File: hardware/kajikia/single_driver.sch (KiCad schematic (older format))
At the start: 17 parts

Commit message: reorder
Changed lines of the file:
@@
 $Descr A4 11693 8268
 encoding utf-8
-Sheet 2 11
+Sheet 6 8
 Title ""
 Date ""
@@
 U 1 1 5AF72EC0
 P 3500 2050
+AR Path="/5AF71FC6/5AF72EC0" Ref="JP1"  Part="1"
+AR Path="/5B406A82/5B411670/5AF72EC0" Ref="JP1"  Part="1"
 F 0 "JP1" H 3500 2255 50  0000 C CNN
 F 1 "SolderJumper_3_Open" H 3500 2164 50  0000 C CNN
@@
 U 1 1 5B028F12
 P 5950 3300
+AR Path="/5AF71FC6/5B028F12" Ref="U?"  Part="1"
+AR Path="/5B406A82/5B411670/5B028F12" Ref="U?"  Part="1"
 F 0 "U?" H 6950 1850 50  0000 C CNN
 F 1 "TMC5160-TA" H 6950 1750 50  0000 C CNN
@@
 U 1 1 5B03C5CD
 P 5950 4900
+AR Path="/5AF71FC6/5B03C5CD" Ref="#PWR0105"  Part="1"
+AR Path="/5B406A82/5B411670/5B03C5CD" Ref="#PWR0105"  Part="1"
 F 0 "#PWR0105" H 5950 4650 50  0001 C CNN
 F 1 "GND" H 5955 4727 50  0000 C CNN
@@
 S 9800 2050 800  1200
 U 5B1A3066
-F0 "stepper_pwr_1" 50
-F1 "stepper_pwr.sch" 50
+F0 "driver_output_1" 50
+F1 "driver_output.sch" 50
 F2 "O1" O R 10600 2150 50
 F3 "O2" O R 10600 2250 50
@@
 S 9800 3600 800  1200
 U 5B1B3F01
-F0 "stepper_pwr_2" 50
-F1 "stepper_pwr.sch" 50
+F0 "driver_output_2" 50
+F1 "driver_output.sch" 50
 F2 "O1" O R 10600 3700 50
 F3 "O2" O R 10600 3800 50
@@
 U 1 1 5B20E949
 P 7200 1500
+AR Path="/5AF71FC6/5B20E949" Ref="C?"  Part="1"
+AR Path="/5B406A82/5B411670/5B20E949" Ref="C?"  Part="1"
 F 0 "C?" H 7225 1600 50  0000 L CNN
 F 1 "100n" H 7225 1400 50  0000 L CNN
@@
 U 1 1 5B20E9BD
 P 6200 1700
+AR Path="/5AF71FC6/5B20E9BD" Ref="C?"  Part="1"
+AR Path="/5B406A82/5B411670/5B20E9BD" Ref="C?"  Part="1"
 F 0 "C?" H 6225 1800 50  0000 L CNN
 F 1 "22n" H 6225 1600 50  0000 L CNN
@@
 U 1 1 5B2161E2
 P 6550 1700
+AR Path="/5AF71FC6/5B2161E2" Ref="C?"  Part="1"
+AR Path="/5B406A82/5B411670/5B2161E2" Ref="C?"  Part="1"
 F 0 "C?" H 6575 1800 50  0000 L CNN
 F 1 "100n" H 6575 1600 50  0000 L CNN
@@
 U 1 1 5B21E5F8
 P 7200 1900
+AR Path="/5AF71FC6/5B21E5F8" Ref="C?"  Part="1"
+AR Path="/5B406A82/5B411670/5B21E5F8" Ref="C?"  Part="1"
 F 0 "C?" H 7225 2000 50  0000 L CNN
 F 1 "2.2u" H 7225 1800 50  0000 L CNN
@@
 U 1 1 5B21E655
 P 7500 1900
+AR Path="/5AF71FC6/5B21E655" Ref="C?"  Part="1"
+AR Path="/5B406A82/5B411670/5B21E655" Ref="C?"  Part="1"
 F 0 "C?" H 7525 2000 50  0000 L CNN
 F 1 "2.2u" H 7525 1800 50  0000 L CNN
@@
 U 1 1 5B2273B4
 P 7800 1750
+AR Path="/5AF71FC6/5B2273B4" Ref="#PWR0106"  Part="1"
+AR Path="/5B406A82/5B411670/5B2273B4" Ref="#PWR0106"  Part="1"
 F 0 "#PWR0106" H 7800 1500 50  0001 C CNN
 F 1 "GND" H 7800 1600 50  0000 C CNN
@@
 U 1 1 5B2486C5
 P 7500 1500
+AR Path="/5AF71FC6/5B2486C5" Ref="C?"  Part="1"
+AR Path="/5B406A82/5B411670/5B2486C5" Ref="C?"  Part="1"
 F 0 "C?" H 7525 1600 50  0000 L CNN
 F 1 "10u" H 7525 1400 50  0000 L CNN
@@
 U 1 1 5B292BDD
 P 4350 1700
+AR Path="/5AF71FC6/5B292BDD" Ref="C?"  Part="1"
+AR Path="/5B406A82/5B411670/5B292BDD" Ref="C?"  Part="1"
 F 0 "C?" H 4375 1800 50  0000 L CNN
 F 1 "22u" H 4375 1600 50  0000 L CNN
@@
 U 1 1 5B29D090
 P 5350 1700
+AR Path="/5AF71FC6/5B29D090" Ref="C?"  Part="1"
+AR Path="/5B406A82/5B411670/5B29D090" Ref="C?"  Part="1"
 F 0 "C?" H 5375 1800 50  0000 L CNN
 F 1 "100n" H 5375 1600 50  0000 L CNN
@@
 U 1 1 5B29D1AE
 P 5100 1700
+AR Path="/5AF71FC6/5B29D1AE" Ref="C?"  Part="1"
+AR Path="/5B406A82/5B411670/5B29D1AE" Ref="C?"  Part="1"
 F 0 "C?" H 5125 1800 50  0000 L CNN
 F 1 "22u" H 5125 1600 50  0000 L CNN
@@
 U 1 1 5B2B2A7E
 P 4600 1700
+AR Path="/5AF71FC6/5B2B2A7E" Ref="C?"  Part="1"
+AR Path="/5B406A82/5B411670/5B2B2A7E" Ref="C?"  Part="1"
 F 0 "C?" H 4625 1800 50  0000 L CNN
 F 1 "100n" H 4625 1600 50  0000 L CNN
@@
 U 1 1 5B2ED34C
 P 4350 2100
+AR Path="/5AF71FC6/5B2ED34C" Ref="#PWR0107"  Part="1"
+AR Path="/5B406A82/5B411670/5B2ED34C" Ref="#PWR0107"  Part="1"
 F 0 "#PWR0107" H 4350 1850 50  0001 C CNN
 F 1 "GND" H 4350 1950 50  0000 C CNN
@@
 U 1 1 5B301C80
 P 7800 1500
+AR Path="/5AF71FC6/5B301C80" Ref="C?"  Part="1"
+AR Path="/5B406A82/5B411670/5B301C80" Ref="C?"  Part="1"
 F 0 "C?" H 7825 1600 50  0000 L CNN
 F 1 "470u" H 7825 1400 50  0000 L CNN
@@
 U 1 1 5B338AD9
 P 3500 3850
+AR Path="/5AF71FC6/5B338AD9" Ref="JP?"  Part="1"
+AR Path="/5B406A82/5B411670/5B338AD9" Ref="JP?"  Part="1"
 F 0 "JP?" H 3400 3750 50  0000 C CNN
 F 1 "SolderJumper_3_Open" H 3500 3960 50  0000 C CNN
@@
 U 1 1 5B338B2F
 P 3500 3400
+AR Path="/5AF71FC6/5B338B2F" Ref="JP?"  Part="1"
+AR Path="/5B406A82/5B411670/5B338B2F" Ref="JP?"  Part="1"
 F 0 "JP?" H 3400 3300 50  0000 C CNN
 F 1 "SolderJumper_3_Open" H 3500 3510 50  0000 C CNN
@@
 U 1 1 5B338BFD
 P 3500 3000
+AR Path="/5AF71FC6/5B338BFD" Ref="JP?"  Part="1"
+AR Path="/5B406A82/5B411670/5B338BFD" Ref="JP?"  Part="1"
 F 0 "JP?" H 3500 3080 50  0000 C CNN
 F 1 "SolderJumper_2_Open" H 3500 2900 50  0000 C CNN
@@
 U 1 1 5B355CF5
 P 3750 3900
+AR Path="/5AF71FC6/5B355CF5" Ref="#PWR0108"  Part="1"
+AR Path="/5B406A82/5B411670/5B355CF5" Ref="#PWR0108"  Part="1"
 F 0 "#PWR0108" H 3750 3650 50  0001 C CNN
 F 1 "GND" H 3750 3750 50  0000 C CNN
@@
 U 1 1 5B39B1CA
 P 3500 2650
+AR Path="/5AF71FC6/5B39B1CA" Ref="JP?"  Part="1"
+AR Path="/5B406A82/5B411670/5B39B1CA" Ref="JP?"  Part="1"
 F 0 "JP?" H 3500 2730 50  0000 C CNN
 F 1 "SolderJumper_2_Open" H 3500 2550 50  0000 C CNN
@@
 U 1 1 5B3EA37B
 P 3750 3450
+AR Path="/5AF71FC6/5B3EA37B" Ref="#PWR0109"  Part="1"
+AR Path="/5B406A82/5B411670/5B3EA37B" Ref="#PWR0109"  Part="1"
 F 0 "#PWR0109" H 3750 3200 50  0001 C CNN
 F 1 "GND" H 3750 3300 50  0000 C CNN

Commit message: io assignments
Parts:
- C10, C11, C12, C13, C14, C15, C16, C17, C18, C19, C9: renamed from C?; footprint (none) -> _Generic:0603_Small
- JP3: renamed from JP1; footprint (none) -> Jumper:SolderJumper-3_P1.3mm_Open_RoundedPad1.0x1.5mm_NumberLabels
- JP4, JP5: renamed from JP?; footprint (none) -> Jumper:SolderJumper-2_P1.3mm_Open_RoundedPad1.0x1.5mm
- JP6, JP7: renamed from JP?; footprint (none) -> Jumper:SolderJumper-3_P1.3mm_Open_RoundedPad1.0x1.5mm_NumberLabels
- U2: renamed from U?; footprint (none) -> Package_QFP:TQFP-48-1EP_7x7mm_P0.5mm_EP3.5x3.5mm

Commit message: switch to tmc5161
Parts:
- removed C10, C12, C14, C15: 100n, _Generic:0603_Small, symbol Device:C
- removed C11, C9: 22u, _Generic:0603_Small, symbol Device:C
- removed C13: 22n, _Generic:0603_Small, symbol Device:C
- removed C16, C18: 2.2u, _Generic:0603_Small, symbol Device:C
- removed C17: 10u, _Generic:0603_Small, symbol Device:C
- removed C19: 470u, _Generic:0603_Small, symbol Device:CP1
- removed JP3, JP6, JP7: SolderJumper_3_Open, Jumper:SolderJumper-3_P1.3mm_Open_RoundedPad1.0x1.5mm_NumberLabels, symbol Jumper:SolderJumper_3_Open
- removed JP4, JP5: SolderJumper_2_Open, Jumper:SolderJumper-2_P1.3mm_Open_RoundedPad1.0x1.5mm, symbol Jumper:SolderJumper_2_Open
- removed U2: TMC5160-TA, Package_QFP:TQFP-48-1EP_7x7mm_P0.5mm_EP3.5x3.5mm, symbol _Personal:TMC5160-TA
- added C? (x5): 470n, symbol Device:C_Small
- added C? (x4): 470p, symbol Device:C_Small
- added C? (x2): 1u, symbol Device:C_Small
- added C? (x4): 100n, symbol Device:C_Small
- added C?: 22n, symbol Device:C_Small
- added C? (x4): 2.2u, symbol Device:C_Small
- added C?: 10u, symbol Device:C_Small
- added D? (x8): D_Schottky_Small, symbol Device:D_Schottky_Small
- added IC?: TMC5161, TMC5161:QFN42L, symbol #Driver_Motor:TMC5161
- added JP? (x2): SolderJumper_2_Open, symbol #PCB_Only:SolderJumper_2_Open
- added R? (x2): 100m, _Generic:0603_Small, symbol Device:R
- added R? (x4): 47, _Generic:0603_Small, symbol Device:R
- added R?: 0, _Generic:0603_Small, symbol Device:R
- added R?: 2.2, symbol Device:R
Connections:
- net labels removed: 5V
- wire segments 164 -> 183
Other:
- note added: "Allow a Zener to drop voltage down"

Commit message: lpc, ios
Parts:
- IC1: renamed from IC?; footprint TMC5161:QFN42L -> footprints:QFN42L
- gave numbers to parts that had none: 39

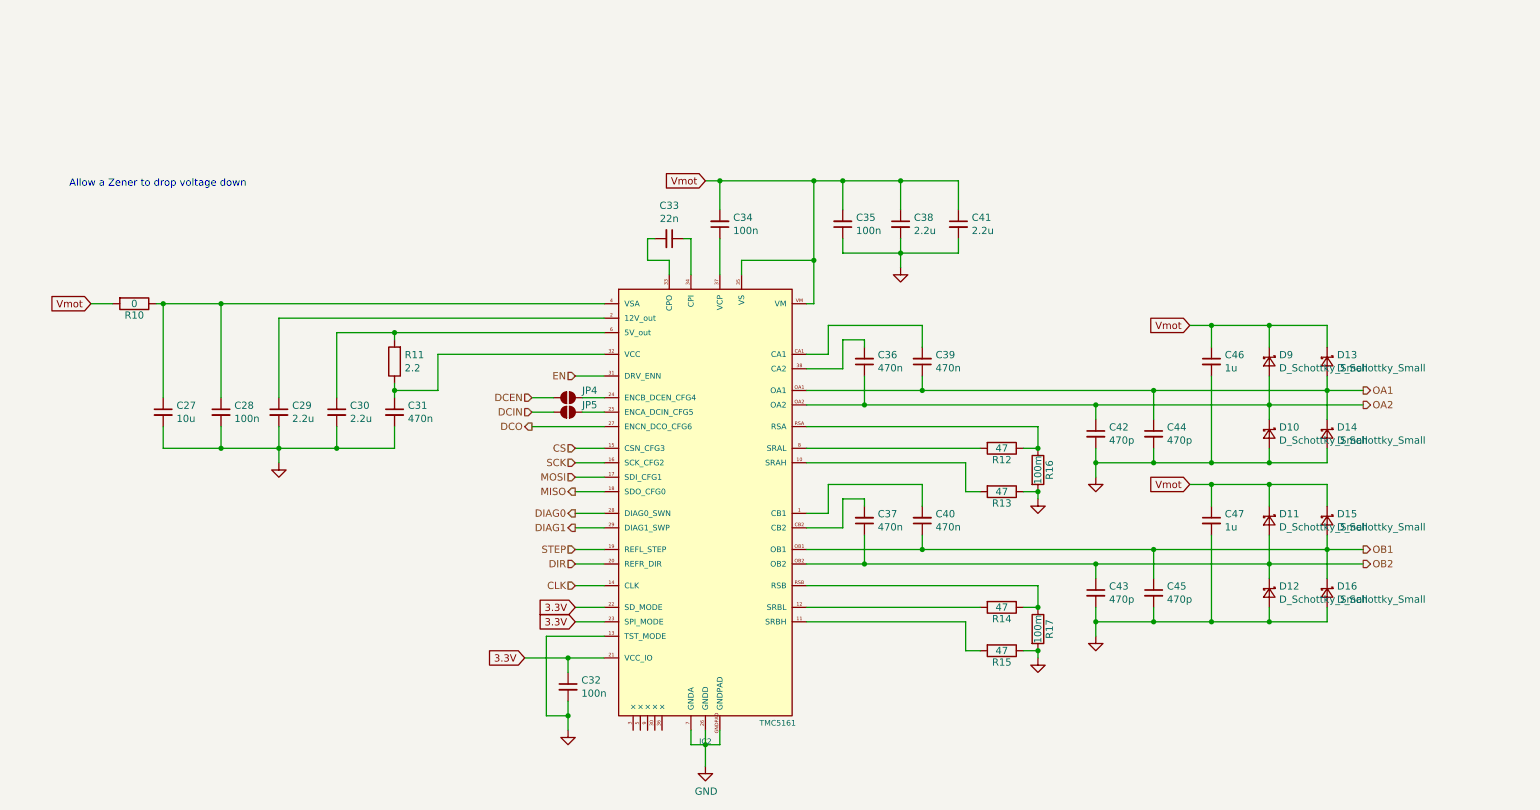
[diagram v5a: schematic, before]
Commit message: max6675, cleanup
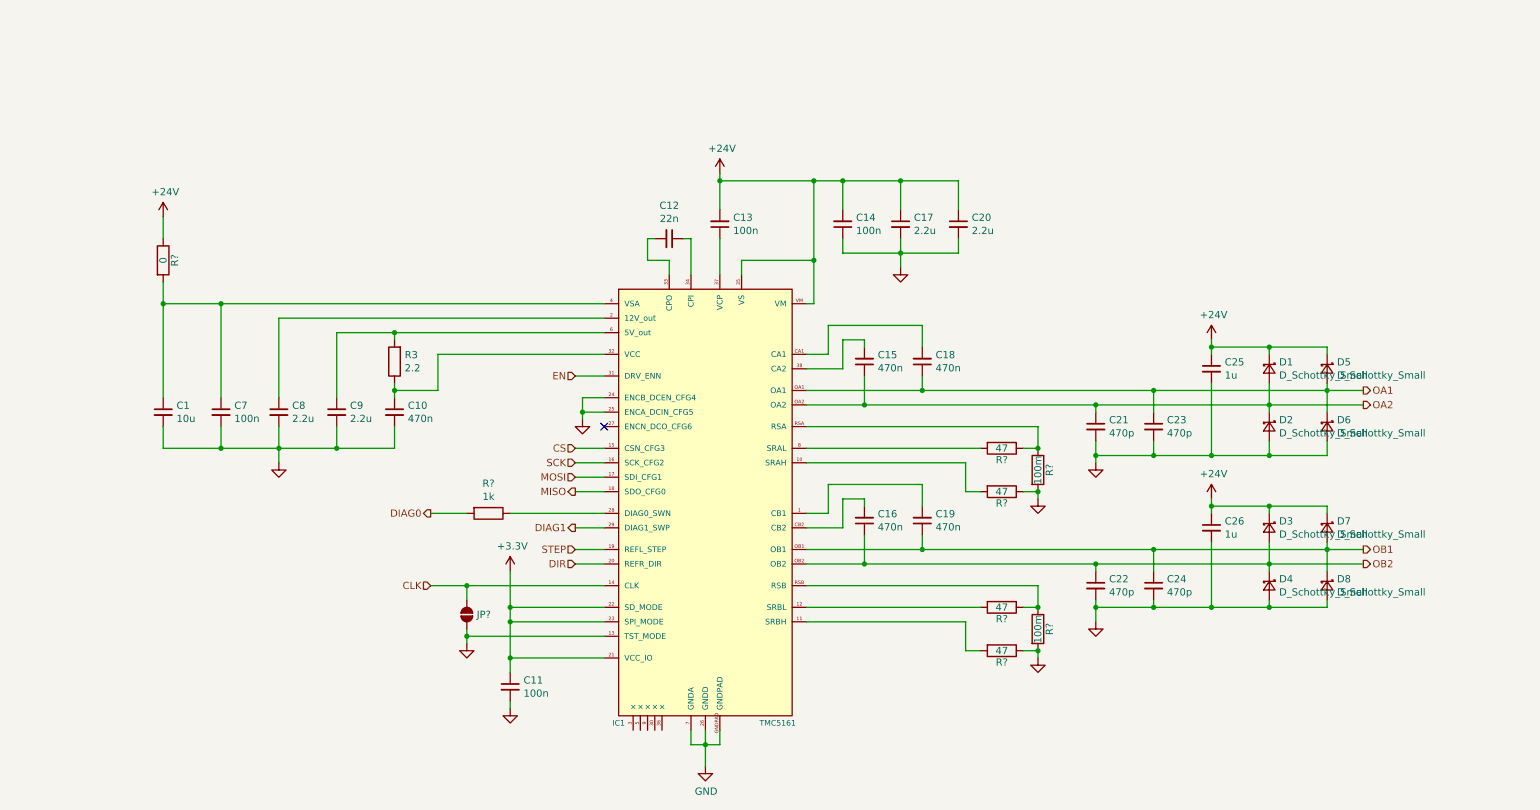
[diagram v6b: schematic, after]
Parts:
- removed JP1, JP3: SolderJumper_2_Open, symbol #PCB_Only:SolderJumper_2_Open
- added JP?: SolderJumper_2_Open, symbol #PCB_Only:SolderJumper_2_Open
- added R?: 1k, symbol Device:R
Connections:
- net CLK: now also JP?.1 (A)
- net DIAG0: now also R?.2; no longer IC1.28 (DIAG0_SWN)
- net GND: now also IC1.24 (ENCB_DCEN_CFG4), IC1.25 (ENCA_DCIN_CFG5), JP?.2 (B)
- net at C1.1, C7.1, IC1.4 (VSA): now also R2.2; no longer R2.1
- net 3.3V renamed +3V3
- net DCO: no longer names the net of IC1.27 (ENCN_DCO_CFG6)
- net Vmot renamed +24V
- net +24V: now also R2.1; no longer R2.2
- new net: IC1.28 (DIAG0_SWN), R?.1
- no-connect marks 0 -> 1
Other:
- note removed: "Allow a Zener to drop voltage down"
- moved on the sheet: C11, C21, C22, C23, C24, C25, C26, D1, D2, D3, D4, D5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

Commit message: power
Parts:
- removed C1: 10u, symbol Device:C_Small
- removed C10: 470n, symbol Device:C_Small
- removed C20: 2.2u, symbol Device:C_Small
- added C181: 470n, symbol Device:C_Small
- added C?: 68u, symbol Device:CP1_Small
- added TP? (x6): TestPoint, symbol #PCB_Only:TestPoint
- C17: value 2.2u -> 4.7u
- C25, C26: value 1u -> 470n
- C7: value 100n -> 10u
- C8: value 2.2u -> 100n
- C9: value 2.2u -> 10u
- D1, D2, D3, D4, D5, D6, D7, D8: value D_Schottky_Small -> MSK4010
- gave numbers to parts that had none: 2
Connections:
- net +24V: now also C?.1; no longer R2.1
- net DIR: now also TP?.1
- net EN: now also TP?.1
- net GND: now also C181.2, C?.2
- net STEP: now also TP?.1
- net at C8.1, IC1.2 (12V_out): now also C7.1, IC1.4 (VSA), R2.2, TP?.1
- net at IC1.32 (VCC), R3.1: now also C181.1, TP?.1
- net at C9.1, IC1.6 (5V_out), R3.2: now also TP?.1
- new net +12V: R2.1
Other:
- moved on the sheet: D41, D42, D43, D44, R85

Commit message: fancy
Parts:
- removed R4, R5, R6, R7: 47, _Generic:0603_Small, symbol Device:R
- removed R8, R9: 100m, _Generic:0603_Small, symbol Device:R
- added R71, R72, R73, R74: 47R, _Generic:0603_RES, symbol Device:R
- added R75, R76: 100m, _Generic:0603_RES, symbol Device:R
- C54: renamed from C7; footprint (none) -> _Generic:0603_CAP
- C55: renamed from C8; footprint (none) -> _Generic:0603_CAP
- C56: renamed from C9; footprint (none) -> _Generic:0603_CAP
- C57: renamed from C181; footprint (none) -> _Generic:0603_CAP
- C58: renamed from C11; footprint (none) -> _Generic:0603_CAP
- C59: renamed from C12; footprint (none) -> _Generic:0603_CAP
- C60: renamed from C13; footprint (none) -> _Generic:0603_CAP
- C61: renamed from C14; footprint (none) -> _Generic:0603_CAP
- C62: renamed from C15; footprint (none) -> _Generic:0603_CAP
- C63: renamed from C16; footprint (none) -> _Generic:0603_CAP
- C64: renamed from C17; footprint (none) -> _Generic:0805_CAP
- C65: renamed from C18; footprint (none) -> _Generic:0603_CAP
- C66: renamed from C19; footprint (none) -> _Generic:0603_CAP
- C68: renamed from C21; footprint (none) -> _Generic:0603_CAP
- C69: renamed from C22; footprint (none) -> _Generic:0603_CAP
- C70: renamed from C23; footprint (none) -> _Generic:0603_CAP
- C71: renamed from C24; footprint (none) -> _Generic:0603_CAP
- C72: renamed from C25; footprint (none) -> _Generic:0603_CAP
- C73: renamed from C26; footprint (none) -> _Generic:0603_CAP
- R68: renamed from R2; value 0 -> 0R; footprint _Generic:0603_Small -> _Generic:0603_RES
- R69: renamed from R3; value 2.2 -> 2.2R; footprint (none) -> _Generic:0603_RES
- R70: renamed from R78; footprint (none) -> _Generic:0603_RES
- gave numbers to parts that had none: 7
- renumbered D1 to D21, D2 to D22, D3 to D23, D4 to D24, D5 to D25, D6 to D26, D7 to D27, D8 to D28, JP36 to JP37
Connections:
- net GND: now also IC1.3 (×), IC1.30 (×), IC1.36 (×), IC1.5 (×), IC1.9 (×), R72.1, R74.1, R75.2, R76.2
- net at IC1.10 (SRAH): now also R72.2
- net at IC1.11 (SRBH): now also R74.2
- net at IC1.12 (SRBL): now also R73.2
- net at IC1.8 (SRAL): now also R71.2
- net at IC1.RSA: now also R71.1, R75.1
- net at IC1.RSB: now also R73.1, R76.1
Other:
- note added: "Stepper Driver"
